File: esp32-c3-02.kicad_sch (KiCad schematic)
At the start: 30 parts, among them J3 GSD090012SEU, U3 ESP32-C3-WROOM-02-H4, U4 CP2102N-Axx-xQFN20, U5 USBLC6-2SC6, U6 W25Q32JVSSIQ

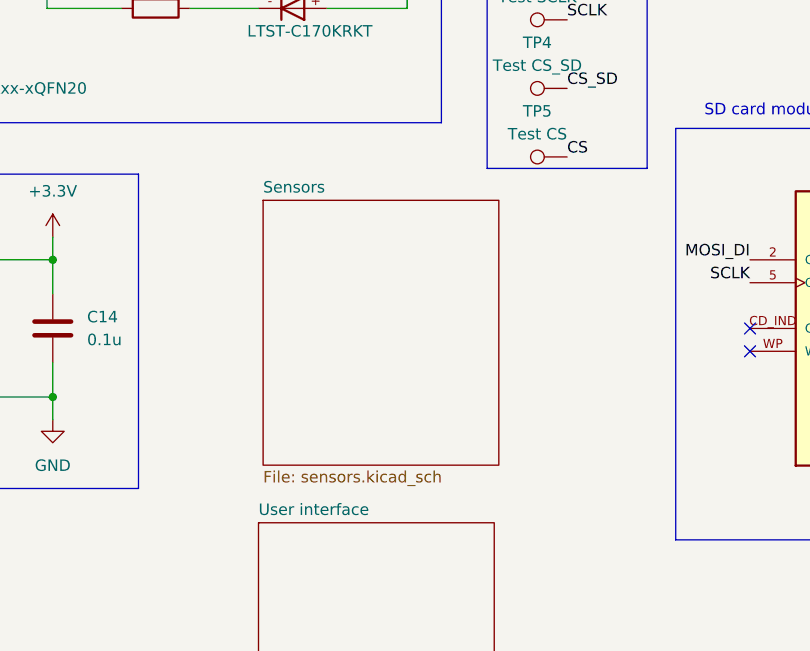
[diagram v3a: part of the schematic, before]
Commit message: 1.3.0 Design the sound sensor subcircuit
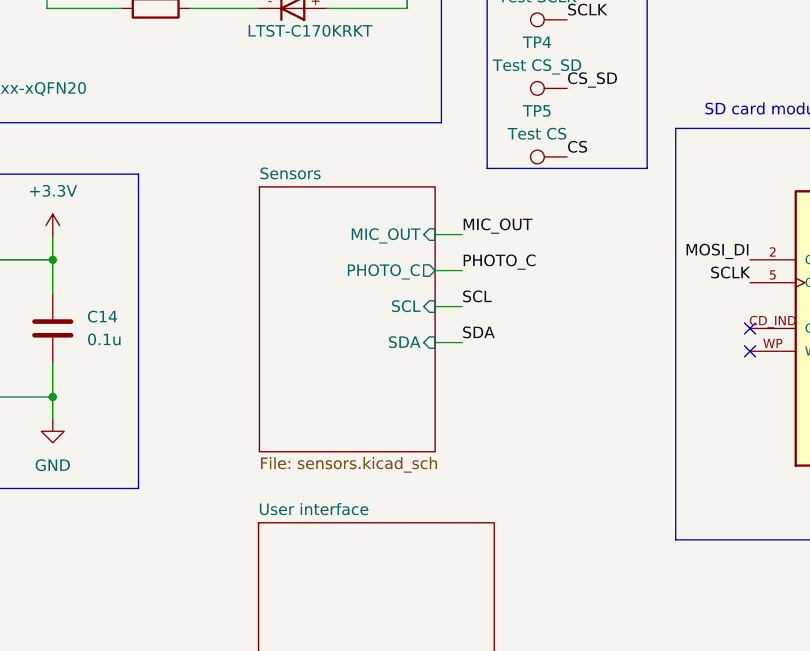
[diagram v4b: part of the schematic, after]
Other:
- sheet Sensors ports: added MIC_OUT, PHOTO_C, SCL, SDA; removed none
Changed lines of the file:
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@@
 	(wire
 		(pts
+			(xy 139 132) (xy 142 132)
+		)
+		(stroke
+			(width 0)
+			(type default)
+		)
+	)
+	(wire
+		(pts
 			(xy 45.72 73.66) (xy 66.04 73.66)
 		)
@@
 	(wire
 		(pts
+			(xy 139 136) (xy 142 136)
+		)
+		(stroke
+			(width 0)
+			(type default)
+		)
+	)
+	(wire
+		(pts
 			(xy 96.52 128.27) (xy 96.52 130.81)
 		)
@@
 	(wire
 		(pts
+			(xy 139 128) (xy 142 128)
+		)
+		(stroke
+			(width 0)
+			(type default)
+		)
+	)
+	(wire
+		(pts
 			(xy 217.17 36.83) (xy 210.82 36.83)
 		)
@@
 	(wire
 		(pts
+			(xy 139 140) (xy 142 140)
+		)
+		(stroke
+			(width 0)
+			(type default)
+		)
+	)
+	(wire
+		(pts
 			(xy 39.37 144.78) (xy 41.91 144.78)
 		)
@@
 		)
 	)
+	(label "MIC_OUT"
+		(at 142 128 0)
+		(effects
+			(font
+				(size 1.27 1.27)
+			)
+			(justify left bottom)
+		)
+	)
 	(label "CS_SD"
 		(at 214.63 138.43 0)
@@
 		)
 	)
+	(label "PHOTO_C"
+		(at 142 132 0)
+		(effects
+			(font
+				(size 1.27 1.27)
+			)
+			(justify left bottom)
+		)
+	)
 	(label "GPIO8"
 		(at 210.82 46.99 0)
@@
 		)
 	)
+	(label "SCL"
+		(at 142 136 0)
+		(effects
+			(font
+				(size 1.27 1.27)
+			)
+			(justify left bottom)
+		)
+	)
 	(label "MISO_DO"
 		(at 153.67 96.52 0)
@@
 		)
 	)
+	(label "SDA"
+		(at 142 140 0)
+		(effects
+			(font
+				(size 1.27 1.27)
+			)
+			(justify left bottom)
+		)
+	)
 	(label "DTS"
 		(at 91.44 66.04 0)
@@
 	)
 	(sheet
-		(at 119.89 124.195)
-		(size 26.19 29.425)
+		(at 119.48 122.705)
+		(size 19.52 29.425)
 		(exclude_from_sim no)
 		(in_bom yes)
@@
 		)
 		(property "Sheetname" "Sensors"
-			(at 119.89 123.4834 0)
+			(at 119.48 121.9934 0)
 			(effects
 				(font
@@
 		)
 		(property "Sheetfile" "sensors.kicad_sch"
-			(at 119.89 154.2046 0)
+			(at 119.48 152.7146 0)
 			(effects
 				(font
@@
 			)
 		)
+		(pin "MIC_OUT" input
+			(at 139 128 0)
+			(effects
+				(font
+					(size 1.27 1.27)
+				)
+				(justify right)
+			)
+		)
+		(pin "PHOTO_C" output
+			(at 139 132 0)
+			(effects
+				(font
+					(size 1.27 1.27)
+				)
+				(justify right)
+			)
+		)
+		(pin "SCL" input
+			(at 139 136 0)
+			(effects
+				(font
+					(size 1.27 1.27)
+				)
+				(justify right)
+			)
+		)
+		(pin "SDA" input
+			(at 139 140 0)
+			(effects
+				(font
+					(size 1.27 1.27)
+				)
+				(justify right)
+			)
+		)

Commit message: 1.3.2 Wiring of the EN and BOOT buttons
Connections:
- net DTS renamed DTR
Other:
- sheet User interface ports: added BOOT, DTR, EN, GPIO18, GPIO19, GPIO8, RTS, SCL, SDA; removed none
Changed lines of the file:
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@@
 		)
 	)
+	(label "SCL"
+		(at 119.38 170.18 180)
+		(effects
+			(font
+				(size 1.27 1.27)
+			)
+			(justify right bottom)
+		)
+	)
 	(label "USB_D-"
 		(at 57.15 73.66 180)
@@
 		)
 	)
+	(label "GPIO19"
+		(at 146.05 180.34 0)
+		(effects
+			(font
+				(size 1.27 1.27)
+			)
+			(justify left bottom)
+		)
+	)
 	(label "BOOT"
 		(at 210.82 49.53 0)
@@
 		)
 	)
+	(label "GPIO8"
+		(at 146.05 175.26 0)
+		(effects
+			(font
+				(size 1.27 1.27)
+			)
+			(justify left bottom)
+		)
+	)
 	(label "PHOTO_C"
 		(at 142 132 0)
@@
 		)
 	)
+	(label "BOOT"
+		(at 119.38 184.15 180)
+		(effects
+			(font
+				(size 1.27 1.27)
+			)
+			(justify right bottom)
+		)
+	)
 	(label "CS_SD"
 		(at 153.67 111.76 0)
@@
 		)
 	)
-	(label "DTS"
+	(label "DTR"
 		(at 91.44 66.04 0)
 		(effects
@@
 		)
 	)
+	(label "SDA"
+		(at 119.38 172.72 180)
+		(effects
+			(font
+				(size 1.27 1.27)
+			)
+			(justify right bottom)
+		)
+	)
 	(label "MOSI_DI"
 		(at 153.67 88.9 0)
@@
 		)
 	)
+	(label "DTR"
+		(at 146.05 165.1 0)
+		(effects
+			(font
+				(size 1.27 1.27)
+			)
+			(justify left bottom)
+		)
+	)
 	(label "SCLK"
 		(at 157.48 59.69 180)
@@
 		)
 	)
+	(label "RTS"
+		(at 146.05 167.64 0)
+		(effects
+			(font
+				(size 1.27 1.27)
+			)
+			(justify left bottom)
+		)
+	)
+	(label "GPIO18"
+		(at 146.05 177.8 0)
+		(effects
+			(font
+				(size 1.27 1.27)
+			)
+			(justify left bottom)
+		)
+	)
+	(label "EN"
+		(at 119.38 181.61 180)
+		(effects
+			(font
+				(size 1.27 1.27)
+			)
+			(justify right bottom)
+		)
+	)
 	(label "EN"
 		(at 175.26 39.37 180)
@@
 	(sheet
 		(at 119.38 160.02)
-		(size 26.19 29.425)
+		(size 26.67 29.21)
 		(exclude_from_sim no)
 		(in_bom yes)
@@
 			)
 		)
+		(pin "BOOT" input
+			(at 119.38 184.15 180)
+			(effects
+				(font
+					(size 1.27 1.27)
+				)
+				(justify left)
+			)
+		)
+		(pin "DTR" output
+			(at 146.05 165.1 0)
+			(effects
+				(font
+					(size 1.27 1.27)
+				)
+				(justify right)
+			)
+		)
+		(pin "EN" input
+			(at 119.38 181.61 180)
+			(effects
+				(font
+					(size 1.27 1.27)
+				)
+				(justify left)
+			)
+		)
+		(pin "GPIO8" bidirectional
+			(at 146.05 175.26 0)
+			(effects
+				(font
+					(size 1.27 1.27)
+				)
+				(justify right)
+			)
+		)
+		(pin "GPIO18" bidirectional
+			(at 146.05 177.8 0)
+			(effects
+				(font
+					(size 1.27 1.27)
+				)
+				(justify right)
+			)
+		)
+		(pin "GPIO19" bidirectional
+			(at 146.05 180.34 0)
+			(effects
+				(font
+					(size 1.27 1.27)
+				)
+				(justify right)
+			)
+		)
+		(pin "RTS" output
+			(at 146.05 167.64 0)
+			(effects
+				(font
+					(size 1.27 1.27)
+				)
+				(justify right)
+			)
+		)
+		(pin "SCL" bidirectional
+			(at 119.38 170.18 180)
+			(effects
+				(font
+					(size 1.27 1.27)
+				)
+				(justify left)
+			)
+		)
+		(pin "SDA" bidirectional
+			(at 119.38 172.72 180)
+			(effects
+				(font
+					(size 1.27 1.27)
+				)
+				(justify left)
+			)
+		)

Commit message: 1.3.3 Symbol and footprint associations
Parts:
- C10, C11, C13, C14, C8: footprint (none) -> Capacitor_SMD:C_0805_2012Metric
- C12, C7, C9: footprint (none) -> ESP32_demo_project:T491A106K010AT7280
- LED5: footprint LED_LTST-C170GKT_LTO -> (none)
- R11, R12, R13, R14, R15, R16, R17, R18, R19, R20: footprint (none) -> Resistor_SMD:R_0805_2012Metric
- TP1, TP2, TP3, TP4, TP5: footprint (none) -> TestPoint:TestPoint_Pad_D1.0mm
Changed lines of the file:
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@@
 			)
 		)
-		(property "Footprint" ""
+		(property "Footprint" "Resistor_SMD:R_0805_2012Metric"
 			(at 107.95 101.092 90)
 			(effects
@@
 			)
 		)
-		(property "Footprint" ""
+		(property "Footprint" "Resistor_SMD:R_0805_2012Metric"
 			(at 107.95 85.852 90)
 			(effects
@@
 			)
 		)
-		(property "Footprint" ""
+		(property "Footprint" "Capacitor_SMD:C_0805_2012Metric"
 			(at 60.96 43.4848 0)
 			(effects
@@
 			)
 		)
-		(property "Footprint" ""
+		(property "Footprint" "Resistor_SMD:R_0805_2012Metric"
 			(at 227.33 136.652 90)
 			(effects
@@
 			)
 		)
-		(property "Footprint" ""
+		(property "Footprint" "Resistor_SMD:R_0805_2012Metric"
 			(at 23.622 64.77 90)
 			(effects
@@
 			)
 		)
-		(property "Footprint" ""
+		(property "Footprint" "Resistor_SMD:R_0805_2012Metric"
 			(at 45.72 143.002 90)
 			(effects
@@
 			)
 		)
-		(property "Footprint" ""
+		(property "Footprint" "Resistor_SMD:R_0805_2012Metric"
 			(at 163.83 61.468 90)
 			(effects
@@
 			)
 		)
-		(property "Footprint" ""
+		(property "Footprint" "TestPoint:TestPoint_Pad_D1.0mm"
 			(at 153.67 99.06 0)
 			(effects
@@
 			)
 		)
-		(property "Footprint" ""
+		(property "Footprint" "TestPoint:TestPoint_Pad_D1.0mm"
 			(at 153.67 114.3 0)
 			(effects
@@
 			)
 		)
-		(property "Footprint" ""
+		(property "Footprint" "Resistor_SMD:R_0805_2012Metric"
 			(at 218.44 129.032 90)
 			(effects
@@
 			)
 		)
-		(property "Footprint" ""
+		(property "Footprint" "TestPoint:TestPoint_Pad_D1.0mm"
 			(at 153.67 83.82 0)
 			(effects
@@
 			)
 		)
-		(property "Footprint" ""
+		(property "Footprint" "ESP32_demo_project:T491A106K010AT7280"
 			(at 53.34 32.7152 0)
 			(effects
@@
 			)
 		)
-		(property "Footprint" ""
+		(property "Footprint" "TestPoint:TestPoint_Pad_D1.0mm"
 			(at 153.67 106.68 0)
 			(effects
@@
 			)
 		)
-		(property "Footprint" "LED_LTST-C170GKT_LTO"
+		(property "Footprint" ""
 			(at 128.27 87.63 0)
 			(effects
@@
 			)
 		)
-		(property "Footprint" ""
+		(property "Footprint" "Capacitor_SMD:C_0805_2012Metric"
 			(at 97.4852 142.24 0)
 			(effects
@@
 			)
 		)
-		(property "Footprint" ""
+		(property "Footprint" "ESP32_demo_project:T491A106K010AT7280"
 			(at 253.6952 49.53 0)
 			(effects
@@
 			)
 		)
-		(property "Footprint" ""
+		(property "Footprint" "ESP32_demo_project:T491A106K010AT7280"
 			(at 254.3048 144.78 0)
 			(effects
@@
 			)
 		)
-		(property "Footprint" ""
+		(property "Footprint" "Capacitor_SMD:C_0805_2012Metric"
 			(at 267.0048 144.78 0)
 			(effects
@@
 			)
 		)
-		(property "Footprint" ""
+		(property "Footprint" "Capacitor_SMD:C_0805_2012Metric"
 			(at 240.9952 49.53 0)
 			(effects
@@
 			)
 		)
-		(property "Footprint" ""
+		(property "Footprint" "Resistor_SMD:R_0805_2012Metric"
 			(at 57.15 60.198 90)
 			(effects
@@
 			)
 		)
-		(property "Footprint" ""
+		(property "Footprint" "Resistor_SMD:R_0805_2012Metric"
 			(at 222.25 42.672 90)
 			(effects
@@
 			)
 		)
-		(property "Footprint" ""
+		(property "Footprint" "Capacitor_SMD:C_0805_2012Metric"
 			(at 37.7952 82.55 0)
 			(effects
@@
 			)
 		)
-		(property "Footprint" ""
+		(property "Footprint" "Resistor_SMD:R_0805_2012Metric"
 			(at 23.622 77.47 90)
 			(effects
@@
 			)
 		)
-		(property "Footprint" ""
+		(property "Footprint" "TestPoint:TestPoint_Pad_D1.0mm"
 			(at 153.67 91.44 0)
 			(effects
